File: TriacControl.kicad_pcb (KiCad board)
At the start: 2 copper layers, 100 x 53 mm, 53 parts, among them J1 AC LINE, J2 LOAD, J3 ZEROCROSS, J4 PWM, Q1 BT136-600, Q2 2N2907, U1 MOC3023, U2 PC817, U3 PC817

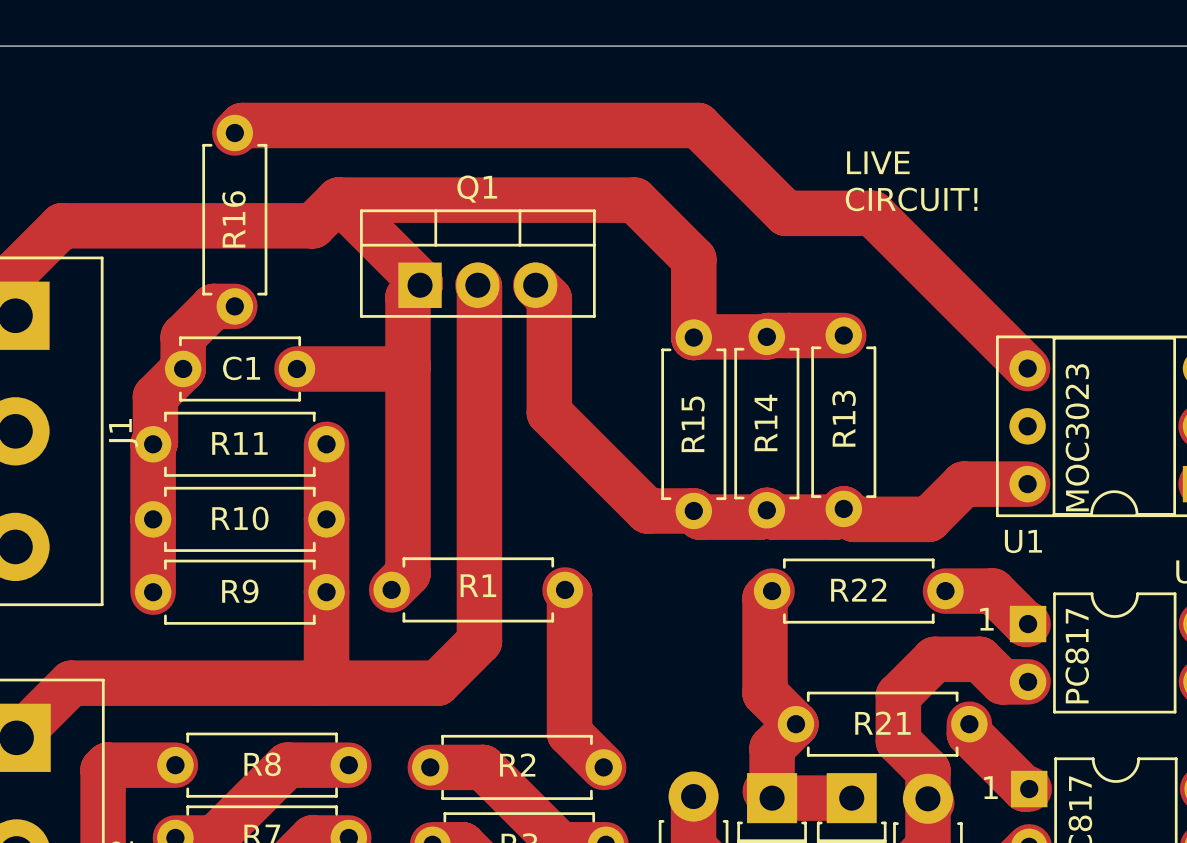
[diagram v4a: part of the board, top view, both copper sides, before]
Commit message: Fixed positioning of component
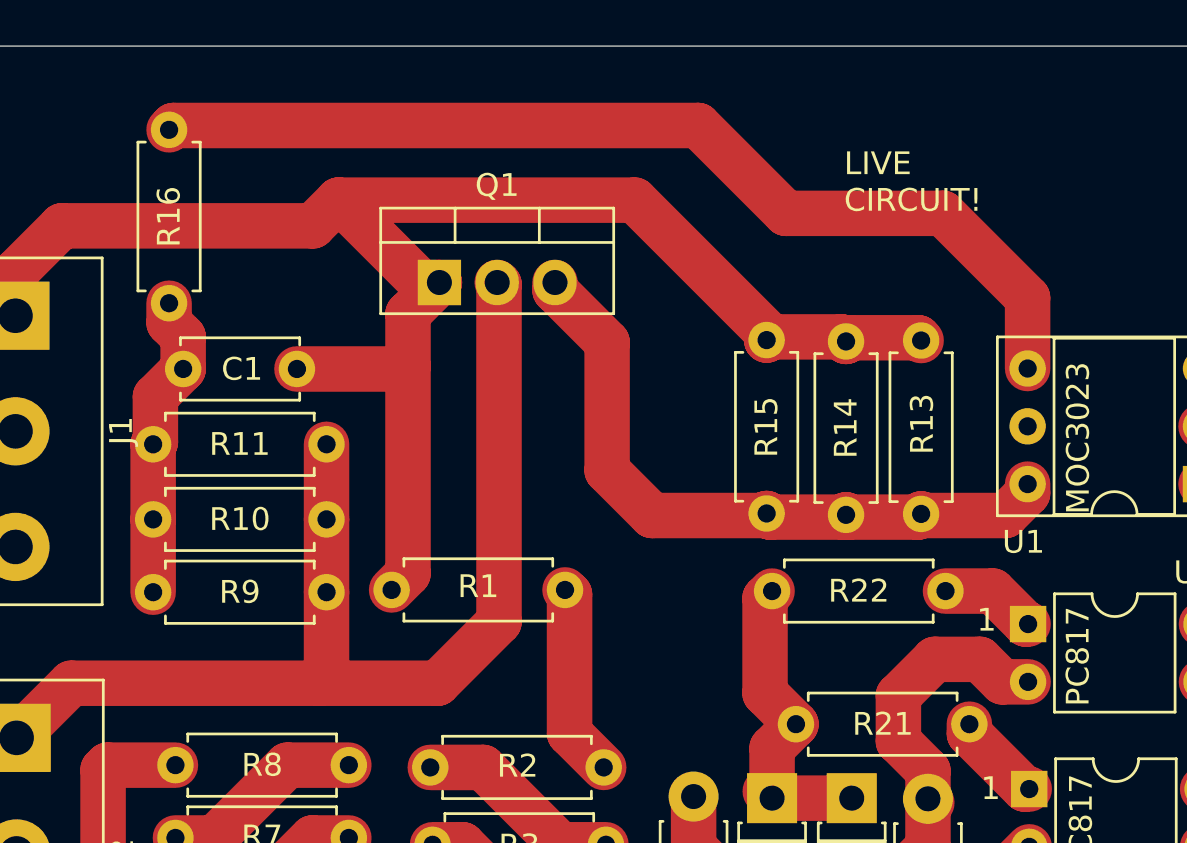
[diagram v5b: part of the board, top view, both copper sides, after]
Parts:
- moved R14 3.49 mm to (94.5, 63.0)
- moved R13 3.41 mm to (97.8, 62.9)
- moved R15 3.20 mm to (91.0, 62.9)
- moved R16 2.89 mm to (64.7, 53.7)
- moved Q1 0.86 mm to (76.6, 60.4)
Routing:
- net Net-(R16-Pad1): track 39.4 -> 44.0 mm
- net Net-(J1-Pin_1): track 68.2 -> 71.3 mm
- net Net-(C1-Pad2): track 14.6 -> 13.5 mm

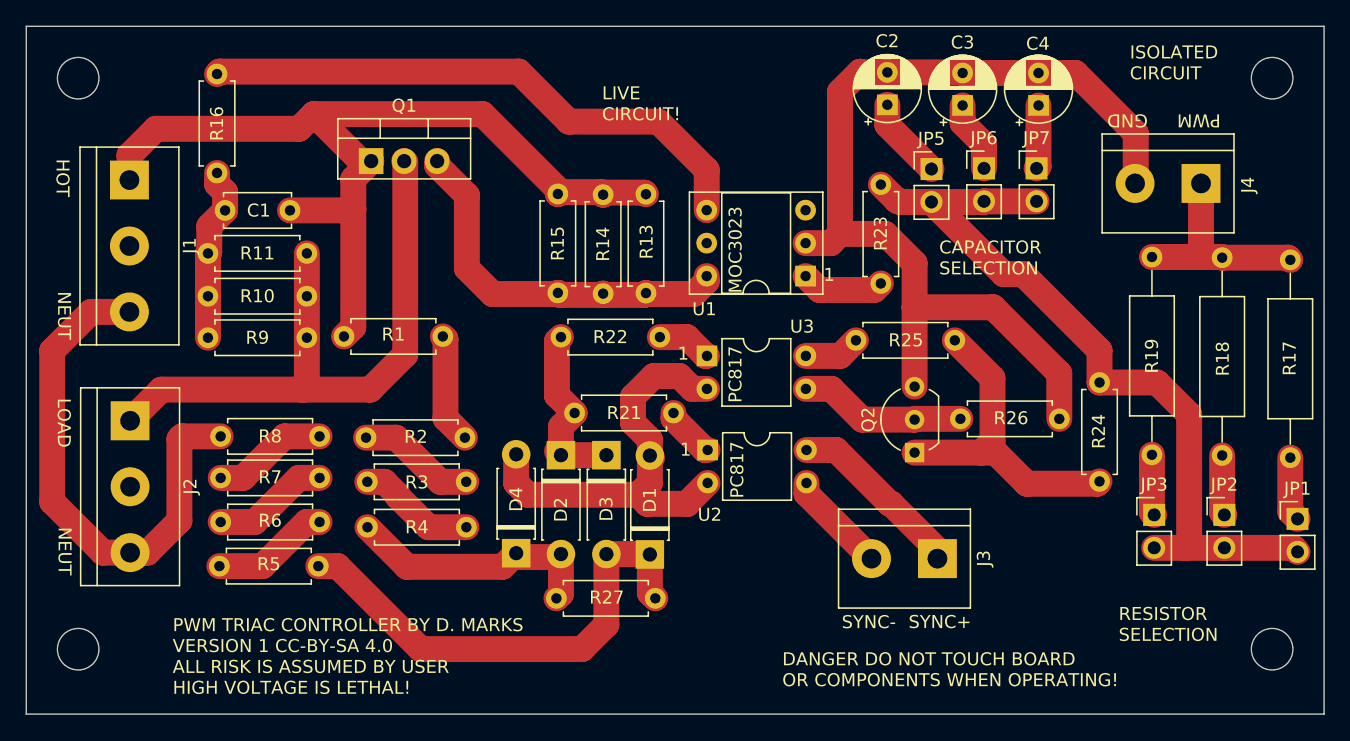
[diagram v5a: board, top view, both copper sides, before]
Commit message: Moved snubber capacitor
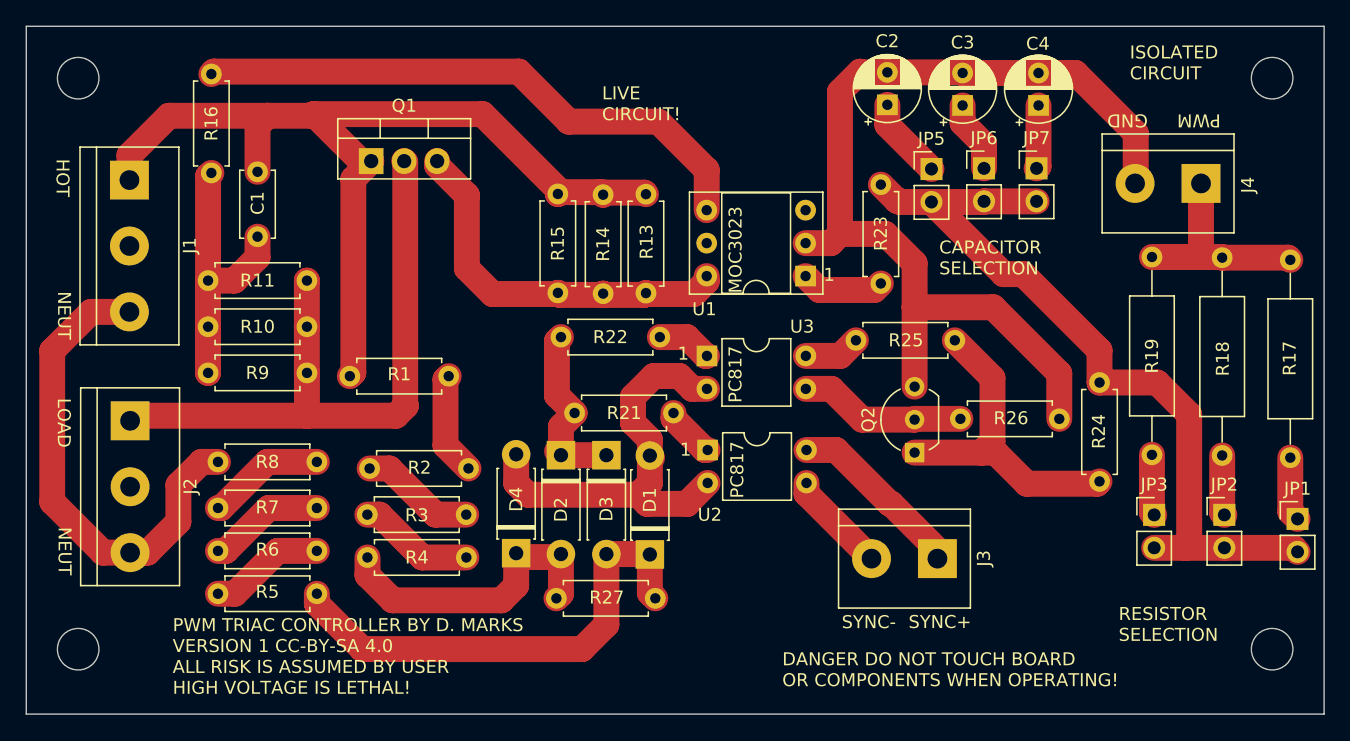
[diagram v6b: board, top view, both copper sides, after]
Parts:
- C1: value 100 nF, 400 V -> 10 nF, 400 V
- Q1: value BT136-600 -> BTA16-600
- R23: value 10R -> 47R
- R24: value 10R -> 4R7
- R25: value 220R -> 47R
- R26: value 2k2 -> 1k
- R27: value 2k2 -> 4k7
- moved C1 3.89 mm to (67.8, 61.2), turned to -90 degrees
- moved R1 3.09 mm to (82.5, 77.0)
- moved R9 2.71 mm to (64.0, 76.7)
- moved R3 2.53 mm to (76.3, 87.6)
- moved R2 2.39 mm to (76.5, 84.1)
- moved R10 2.35 mm to (64.0, 73.2)
- moved R4 2.33 mm to (76.3, 90.9)
- moved R7 2.33 mm to (72.4, 87.1)
- moved R6 2.23 mm to (72.4, 90.4)
- moved R5 2.13 mm to (72.4, 93.7)
- moved R11 2.10 mm to (64.0, 69.6)
- moved R8 1.98 mm to (72.4, 83.6)
- moved R16 0.44 mm to (64.3, 53.7)
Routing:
- net Net-(C1-Pad2): track 13.5 -> 21.8 mm
- net Net-(D2-A): track 20.4 -> 23.8 mm
- net Net-(J1-Pin_3): track 40.8 -> 37.8 mm
- net Net-(J1-Pin_1): track 71.3 -> 73.9 mm
- net Net-(J2-Pin_1): track 48.9 -> 51.1 mm
- net Net-(R1-Pad1): track 8.50 -> 7.95 mm

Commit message: Moved components a little ore
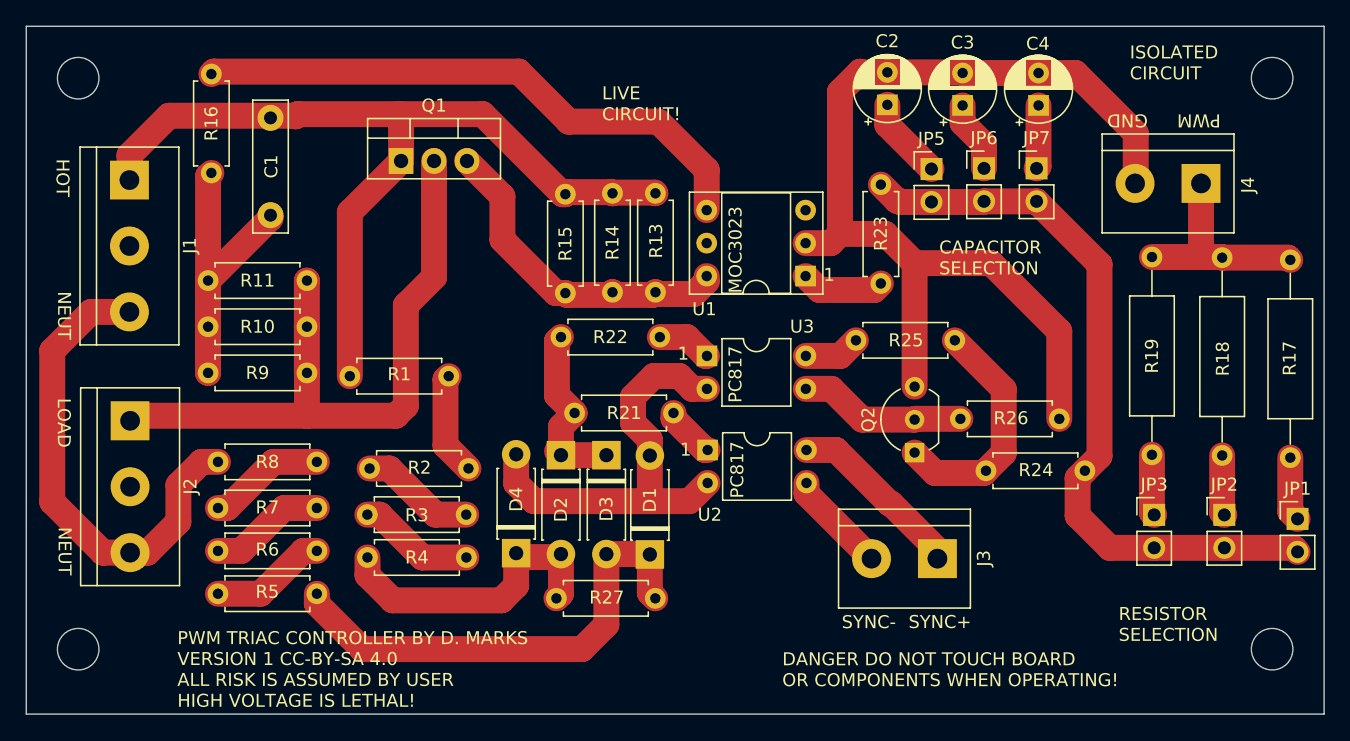
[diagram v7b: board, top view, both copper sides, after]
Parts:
- C1: footprint Capacitor_THT:C_Disc_D5.0mm_W2.5mm_P5.00mm -> Capacitor_THT:C_Rect_L10.0mm_W2.5mm_P7.50mm_MKS4
- moved R24 6.89 mm to (131.6, 84.2), turned to 180 degrees
- moved C1 4.27 mm to (68.8, 57.1)
- moved Q1 2.30 mm to (78.9, 60.4)
- moved R13 0.73 mm to (98.5, 62.9)
- moved R14 0.73 mm to (95.2, 62.9)
- moved R15 0.58 mm to (91.5, 62.9)
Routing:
- net Net-(Q2-E): track 25.5 -> 18.4 mm
- net Net-(J1-Pin_1): track 73.9 -> 68.4 mm
- net Net-(JP1-B): track 62.2 -> 57.6 mm
- net Net-(Q1-G): track 29.6 -> 25.8 mm
- net GND2: track 76.2 -> 79.5 mm
- net Net-(J2-Pin_1): track 51.1 -> 51.9 mm
- net Net-(C1-Pad2): track 21.8 -> 22.6 mm

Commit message: Added snubber capacitor calculation
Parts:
- R10, R9: value 100R -> 22k
- R11: value 100R -> NC
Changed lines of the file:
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@@
         (effects (font (size 1 1) (thickness 0.15)))
     )
-    (fp_text value "100R" (at 3.81 2.37) (layer "F.Fab")
+    (fp_text value "22k" (at 3.81 2.37) (layer "F.Fab")
         (effects (font (size 1 1) (thickness 0.15)))
     )
@@
         (effects (font (size 1 1) (thickness 0.15)))
     )
-    (fp_text value "100R" (at 3.81 2.37) (layer "F.Fab")
+    (fp_text value "NC" (at 3.81 2.37) (layer "F.Fab")
         (effects (font (size 1 1) (thickness 0.15)))
     )
@@
         (effects (font (size 1 1) (thickness 0.15)))
     )
-    (fp_text value "100R" (at 3.81 2.37) (layer "F.Fab")
-        (effects (font (size 1 1) (thickness 0.15)))
-    )
+    (fp_text value "22k" (at 3.81 2.37) (layer "F.Fab")
+        (effects (font (size 1 1) (thickness 0.15)))
+    )
